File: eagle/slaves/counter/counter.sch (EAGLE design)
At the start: 92 parts, among them IC1 MCP1703DB, IC2 4067D, IC3 74HC154DW, J1 RJ12RIGHTANGLE-I2C, X2 8MHz, X4 MINI-USB

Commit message: change resistor for led
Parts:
- RK11, RK13, RK17, RK19, RK21, RK23, RK25, RK27, RK29, RK31, RK33, RK35, RK41, RK43, RK5, RK9: value 1k -> 100
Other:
- moved on the sheet: C14, C15, C18, C19, C7, C8, O10, O13, O14, O5, O6, O9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

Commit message: remove 10nf capacitor
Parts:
- removed C11, C14, C15, C16, C17, C18, C19, C20, C21, C24, C25, C5, C6, C7, C8, C9: 10n, rcl:C-EUC0805
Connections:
- net 3.3V: no longer C11.2, C14.2, C15.2, C16.2, C17.2, C18.2, C19.2, C20.2, C21.2, C24.2, C25.2, C5.2, C6.2, C7.2, C8.2, C9.2
- net Y10: no longer C15.1
- net Y11: no longer C16.1
- net Y12: no longer C17.1
- net Y13: no longer C18.1
- net Y14: no longer C19.1
- net Y15: no longer C20.1
- net Y16: no longer C21.1
- net Y19: no longer C24.1
- net Y20: no longer C25.1
- net Y3: no longer C5.1
- net Y4: no longer C6.1
- net Y5: no longer C7.1
- net Y6: no longer C8.1
- net Y7: no longer C9.1
- net Y8: no longer C11.1
- net Y9: no longer C14.1

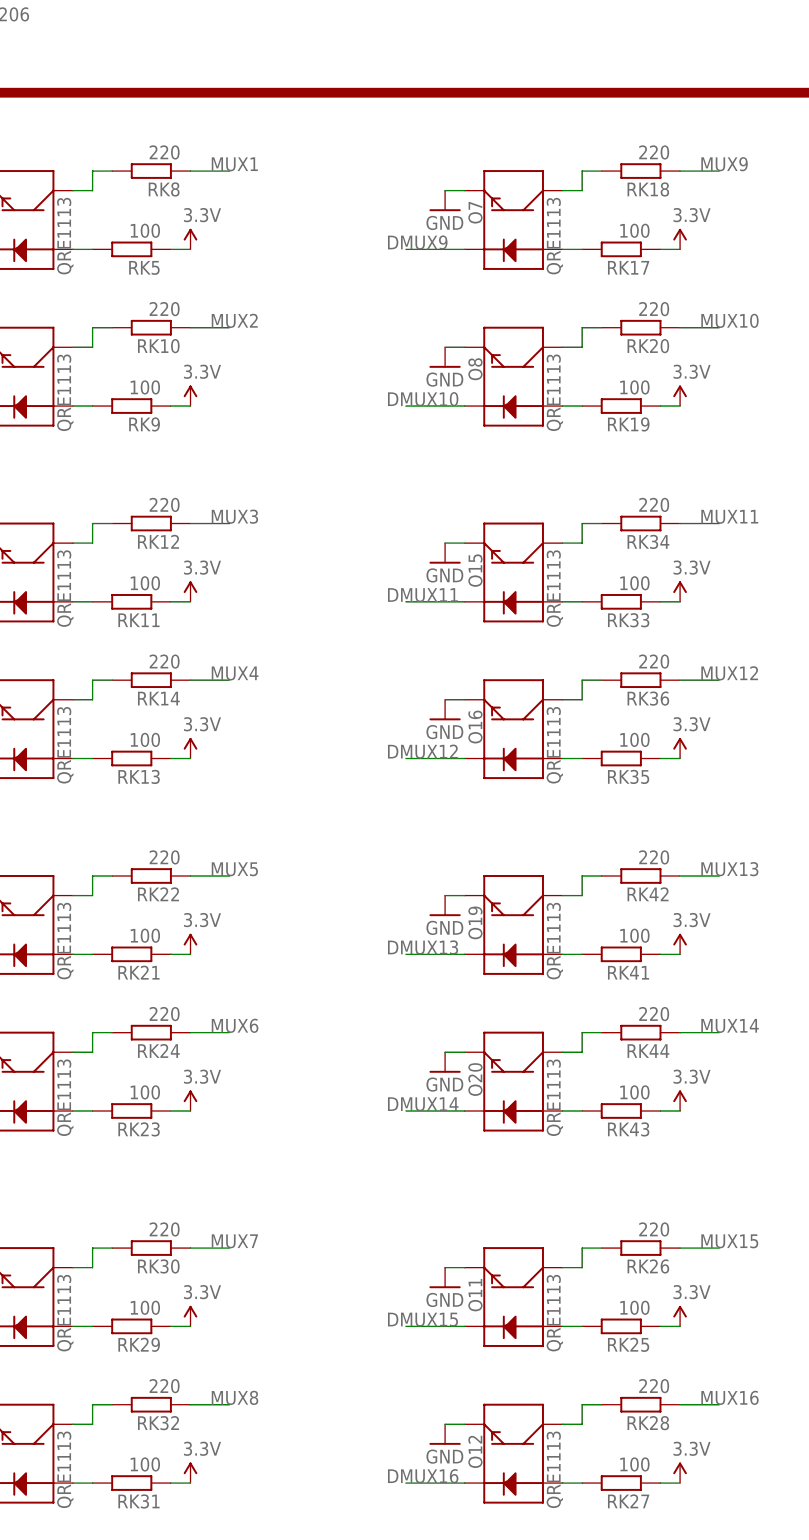
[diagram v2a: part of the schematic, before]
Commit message: change resistor to 1k
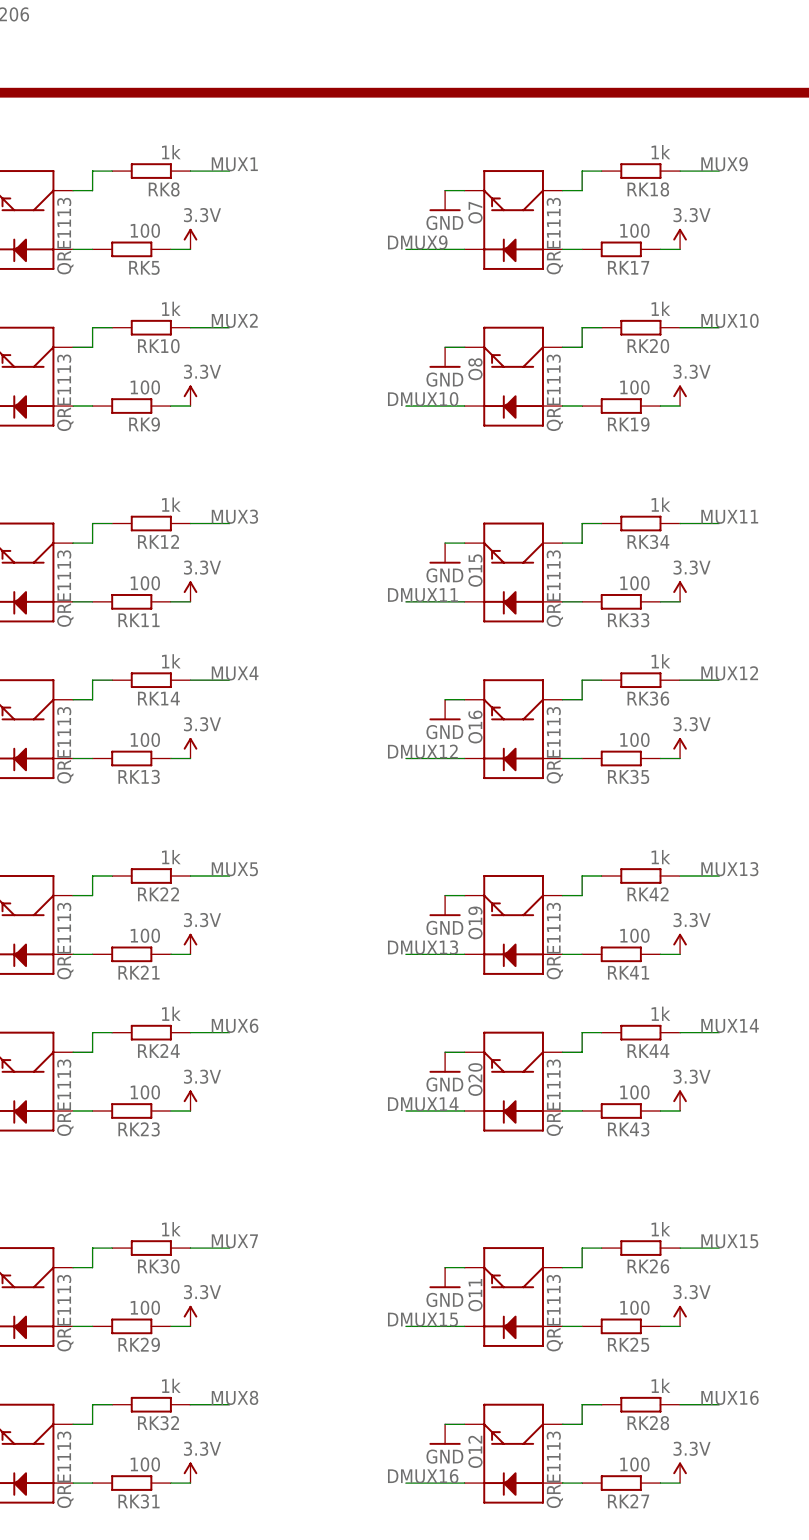
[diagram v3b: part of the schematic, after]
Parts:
- RK10, RK12, RK14, RK18, RK20, RK22, RK24, RK26, RK28, RK30, RK32, RK34, RK36, RK42, RK44, RK8: value 220 -> 1k
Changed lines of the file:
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@@
 <part name="P+13" library="SparkFun" deviceset="3.3V" device=""/>
 <part name="GND16" library="supply1" deviceset="GND" device=""/>
-<part name="RK8" library="resistor" deviceset="R-EU_" device="M0805" value="220"/>
+<part name="RK8" library="resistor" deviceset="R-EU_" device="M0805" value="1k"/>
 <part name="O4" library="SparkFun" deviceset="QRE1113" device=""/>
 <part name="RK9" library="resistor" deviceset="R-EU_" device="M0805" value="100"/>
 <part name="P+14" library="SparkFun" deviceset="3.3V" device=""/>
 <part name="GND17" library="supply1" deviceset="GND" device=""/>
-<part name="RK10" library="resistor" deviceset="R-EU_" device="M0805" value="220"/>
+<part name="RK10" library="resistor" deviceset="R-EU_" device="M0805" value="1k"/>
 <part name="O5" library="SparkFun" deviceset="QRE1113" device=""/>
 <part name="RK11" library="resistor" deviceset="R-EU_" device="M0805" value="100"/>
 <part name="P+7" library="SparkFun" deviceset="3.3V" device=""/>
 <part name="GND11" library="supply1" deviceset="GND" device=""/>
-<part name="RK12" library="resistor" deviceset="R-EU_" device="M0805" value="220"/>
+<part name="RK12" library="resistor" deviceset="R-EU_" device="M0805" value="1k"/>
 <part name="O6" library="SparkFun" deviceset="QRE1113" device=""/>
 <part name="RK13" library="resistor" deviceset="R-EU_" device="M0805" value="100"/>
 <part name="P+10" library="SparkFun" deviceset="3.3V" device=""/>
 <part name="GND13" library="supply1" deviceset="GND" device=""/>
-<part name="RK14" library="resistor" deviceset="R-EU_" device="M0805" value="220"/>
+<part name="RK14" library="resistor" deviceset="R-EU_" device="M0805" value="1k"/>
 <part name="O9" library="SparkFun" deviceset="QRE1113" device=""/>
 <part name="RK21" library="resistor" deviceset="R-EU_" device="M0805" value="100"/>
 <part name="P+17" library="SparkFun" deviceset="3.3V" device=""/>
 <part name="GND22" library="supply1" deviceset="GND" device=""/>
-<part name="RK22" library="resistor" deviceset="R-EU_" device="M0805" value="220"/>
+<part name="RK22" library="resistor" deviceset="R-EU_" device="M0805" value="1k"/>
 <part name="O10" library="SparkFun" deviceset="QRE1113" device=""/>
 <part name="RK23" library="resistor" deviceset="R-EU_" device="M0805" value="100"/>
 <part name="P+19" library="SparkFun" deviceset="3.3V" device=""/>
 <part name="GND23" library="supply1" deviceset="GND" device=""/>
-<part name="RK24" library="resistor" deviceset="R-EU_" device="M0805" value="220"/>
+<part name="RK24" library="resistor" deviceset="R-EU_" device="M0805" value="1k"/>
 <part name="O13" library="SparkFun" deviceset="QRE1113" device=""/>
 <part name="RK29" library="resistor" deviceset="R-EU_" device="M0805" value="100"/>
 <part name="P+24" library="SparkFun" deviceset="3.3V" device=""/>
 <part name="GND28" library="supply1" deviceset="GND" device=""/>
-<part name="RK30" library="resistor" deviceset="R-EU_" device="M0805" value="220"/>
+<part name="RK30" library="resistor" deviceset="R-EU_" device="M0805" value="1k"/>
 <part name="O14" library="SparkFun" deviceset="QRE1113" device=""/>
 <part name="RK31" library="resistor" deviceset="R-EU_" device="M0805" value="100"/>
 <part name="P+25" library="SparkFun" deviceset="3.3V" device=""/>
 <part name="GND29" library="supply1" deviceset="GND" device=""/>
-<part name="RK32" library="resistor" deviceset="R-EU_" device="M0805" value="220"/>
+<part name="RK32" library="resistor" deviceset="R-EU_" device="M0805" value="1k"/>
 <part name="O7" library="SparkFun" deviceset="QRE1113" device=""/>
 <part name="RK17" library="resistor" deviceset="R-EU_" device="M0805" value="100"/>
 <part name="P+3" library="SparkFun" deviceset="3.3V" device=""/>
 <part name="GND5" library="supply1" deviceset="GND" device=""/>
-<part name="RK18" library="resistor" deviceset="R-EU_" device="M0805" value="220"/>
+<part name="RK18" library="resistor" deviceset="R-EU_" device="M0805" value="1k"/>
 <part name="O8" library="SparkFun" deviceset="QRE1113" device=""/>
 <part name="RK19" library="resistor" deviceset="R-EU_" device="M0805" value="100"/>
 <part name="P+4" library="SparkFun" deviceset="3.3V" device=""/>
 <part name="GND6" library="supply1" deviceset="GND" device=""/>
-<part name="RK20" library="resistor" deviceset="R-EU_" device="M0805" value="220"/>
+<part name="RK20" library="resistor" deviceset="R-EU_" device="M0805" value="1k"/>
 <part name="O15" library="SparkFun" deviceset="QRE1113" device=""/>
 <part name="RK33" library="resistor" deviceset="R-EU_" device="M0805" value="100"/>
 <part name="P+16" library="SparkFun" deviceset="3.3V" device=""/>
 <part name="GND24" library="supply1" deviceset="GND" device=""/>
-<part name="RK34" library="resistor" deviceset="R-EU_" device="M0805" value="220"/>
+<part name="RK34" library="resistor" deviceset="R-EU_" device="M0805" value="1k"/>
 <part name="O16" library="SparkFun" deviceset="QRE1113" device=""/>
 <part name="RK35" library="resistor" deviceset="R-EU_" device="M0805" value="100"/>
 <part name="P+22" library="SparkFun" deviceset="3.3V" device=""/>
 <part name="GND26" library="supply1" deviceset="GND" device=""/>
-<part name="RK36" library="resistor" deviceset="R-EU_" device="M0805" value="220"/>
+<part name="RK36" library="resistor" deviceset="R-EU_" device="M0805" value="1k"/>
 <part name="O19" library="SparkFun" deviceset="QRE1113" device=""/>
 <part name="RK41" library="resistor" deviceset="R-EU_" device="M0805" value="100"/>
 <part name="P+27" library="SparkFun" deviceset="3.3V" device=""/>
 <part name="GND33" library="supply1" deviceset="GND" device=""/>
-<part name="RK42" library="resistor" deviceset="R-EU_" device="M0805" value="220"/>
+<part name="RK42" library="resistor" deviceset="R-EU_" device="M0805" value="1k"/>
 <part name="O20" library="SparkFun" deviceset="QRE1113" device=""/>
 <part name="RK43" library="resistor" deviceset="R-EU_" device="M0805" value="100"/>
 <part name="P+29" library="SparkFun" deviceset="3.3V" device=""/>
 <part name="GND34" library="supply1" deviceset="GND" device=""/>
-<part name="RK44" library="resistor" deviceset="R-EU_" device="M0805" value="220"/>
+<part name="RK44" library="resistor" deviceset="R-EU_" device="M0805" value="1k"/>
 <part name="O11" library="SparkFun" deviceset="QRE1113" device=""/>
 <part name="RK25" library="resistor" deviceset="R-EU_" device="M0805" value="100"/>
 <part name="P+5" library="SparkFun" deviceset="3.3V" device=""/>
 <part name="GND9" library="supply1" deviceset="GND" device=""/>
-<part name="RK26" library="resistor" deviceset="R-EU_" device="M0805" value="220"/>
+<part name="RK26" library="resistor" deviceset="R-EU_" device="M0805" value="1k"/>
 <part name="O12" library="SparkFun" deviceset="QRE1113" device=""/>
 <part name="RK27" library="resistor" deviceset="R-EU_" device="M0805" value="100"/>
 <part name="P+6" library="SparkFun" deviceset="3.3V" device=""/>
 <part name="GND10" library="supply1" deviceset="GND" device=""/>
-<part name="RK28" library="resistor" deviceset="R-EU_" device="M0805" value="220"/>
+<part name="RK28" library="resistor" deviceset="R-EU_" device="M0805" value="1k"/>
 </parts>
 <sheets>
